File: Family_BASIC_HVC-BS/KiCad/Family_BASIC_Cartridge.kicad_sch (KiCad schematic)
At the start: 19 parts, among them IC1 Working RAM (62256), IC2 Program ROM (27256), IC3 74HCT20, IC4 Character ROM (2764), SW1 BACKUP SW, SW2 RAM BANK SW

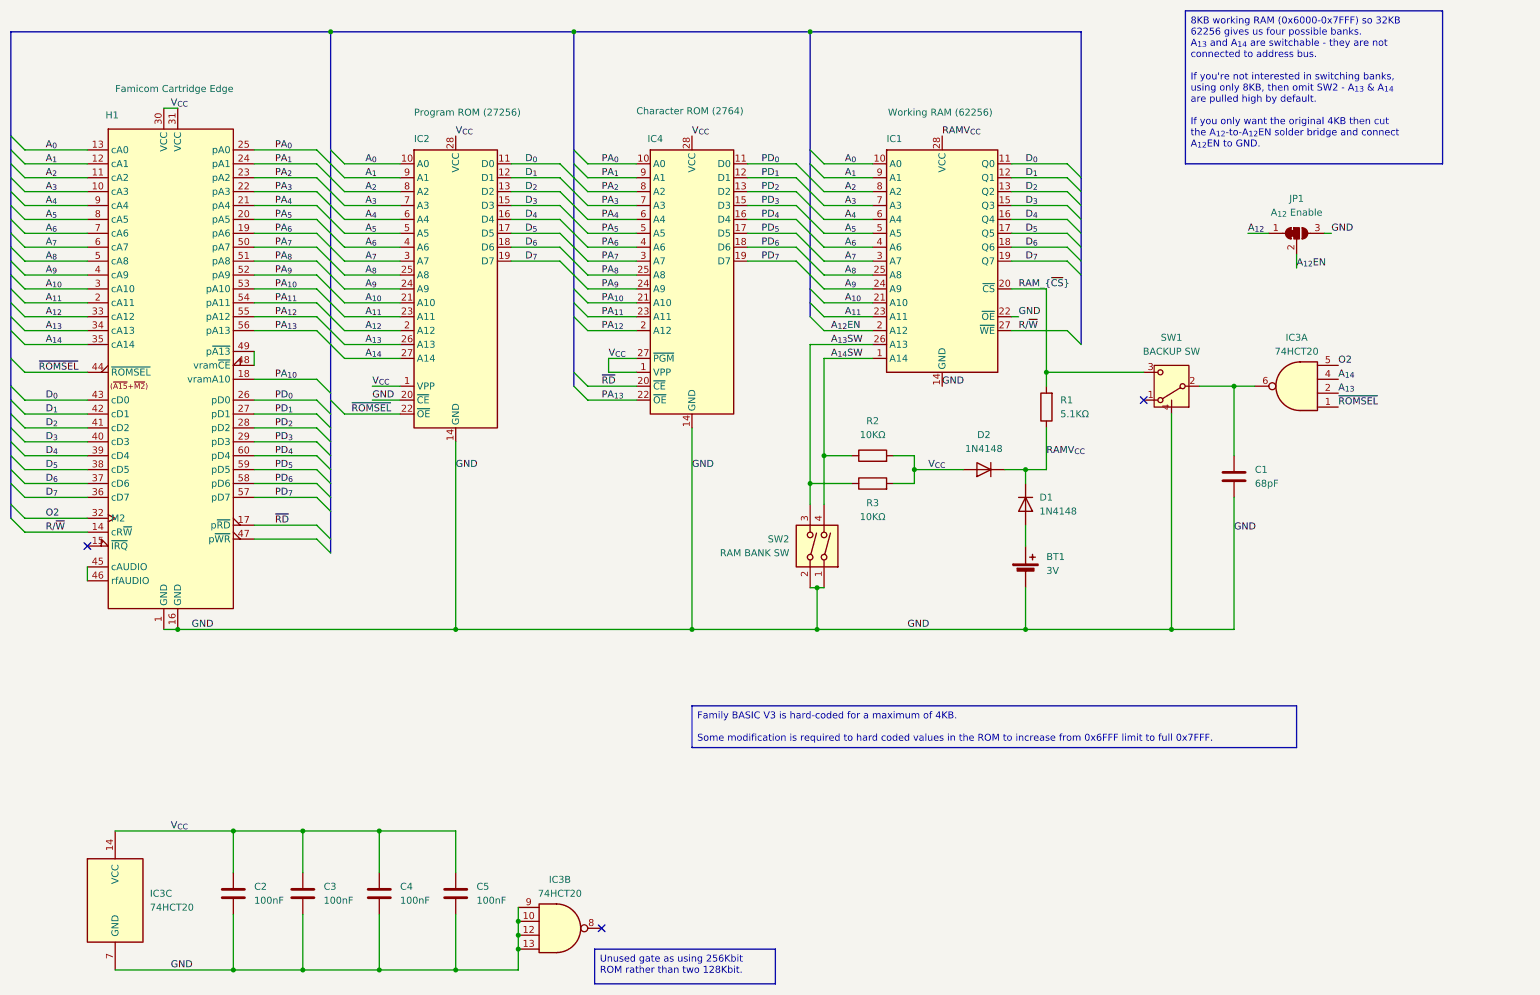
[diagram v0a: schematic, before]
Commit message: Switchable BASIC version with 27512
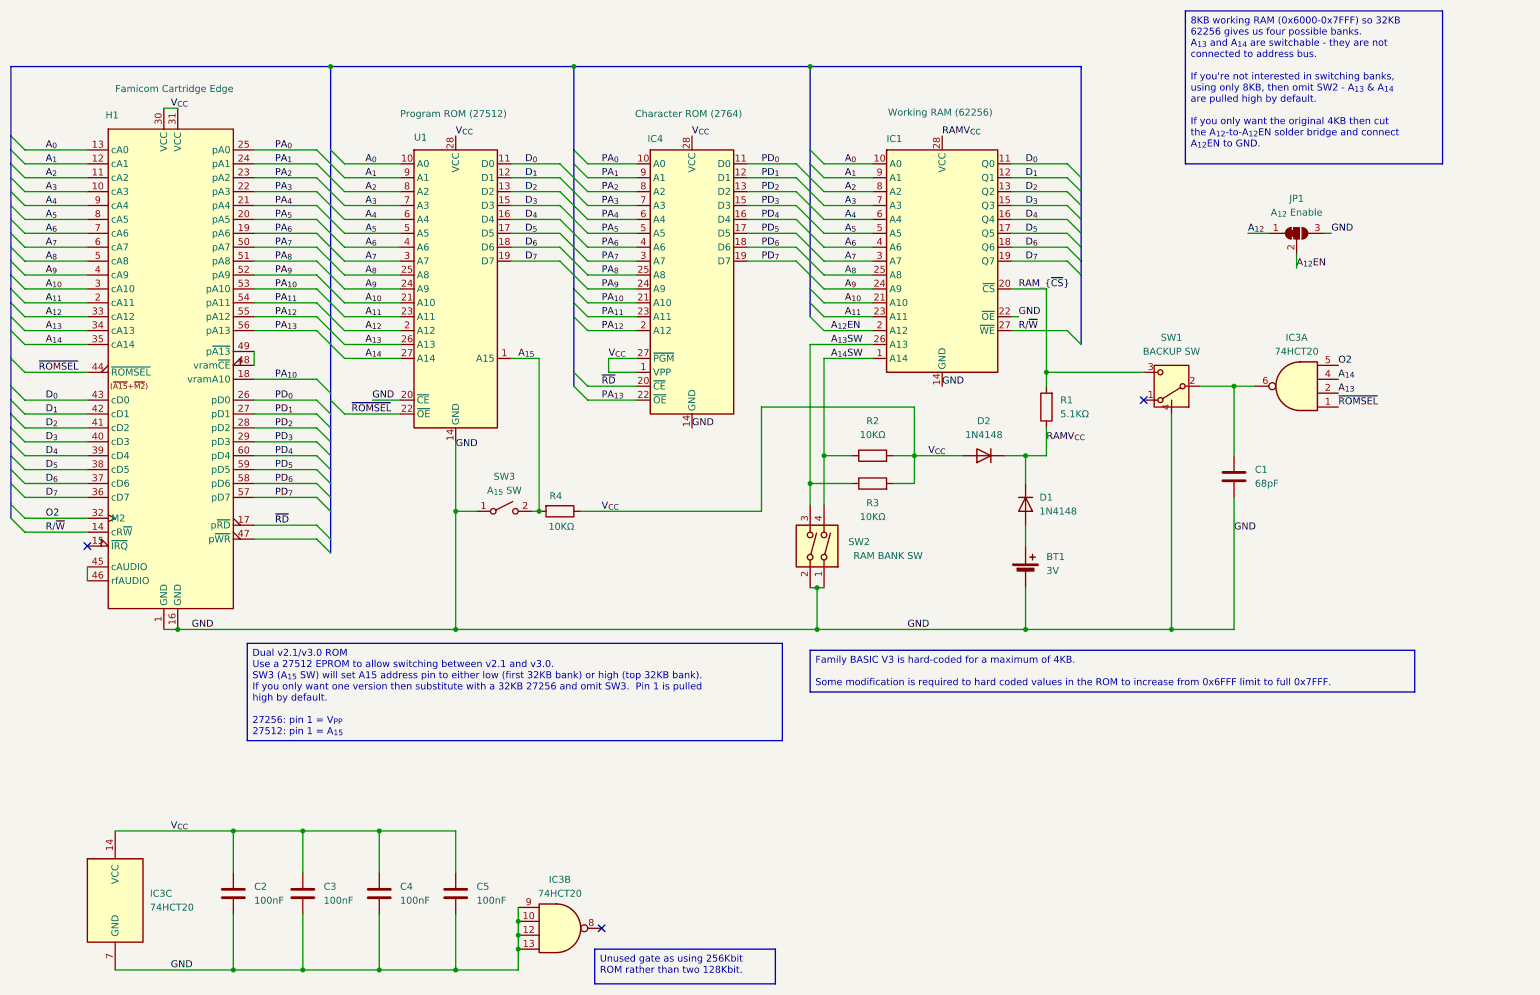
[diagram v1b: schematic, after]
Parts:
- removed IC2: Program ROM (27256), Package_DIP:DIP-28_W15.24mm, symbol Memory_EPROM:27C256
- added R4: 10KΩ, Resistor_THT:R_Axial_DIN0207_L6.3mm_D2.5mm_P7.62mm_Horizontal, symbol Device:R
- added SW3: A_{15} SW, symbol Switch:SW_SPST
- added U1: Program ROM (27512), Package_DIP:DIP-28_W15.24mm, symbol Memory_EPROM:27C512
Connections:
- net A_{0}: now also U1.10 (A0)
- net A_{10}: now also U1.21 (A10)
- net A_{11}: now also U1.23 (A11)
- net A_{12}: now also U1.2 (A12)
- net A_{13}: now also U1.26 (A13)
- net A_{14}: now also U1.27 (A14)
- net A_{1}: now also U1.9 (A1)
- net A_{2}: now also U1.8 (A2)
- net A_{3}: now also U1.7 (A3)
- net A_{4}: now also U1.6 (A4)
- net A_{5}: now also U1.5 (A5)
- net A_{6}: now also U1.4 (A6)
- net A_{7}: now also U1.3 (A7)
- net A_{8}: now also U1.25 (A8)
- net A_{9}: now also U1.24 (A9)
- net D_{0}: now also U1.11 (D0)
- net D_{1}: now also U1.12 (D1)
- net D_{2}: now also U1.13 (D2)
- net D_{3}: now also U1.15 (D3)
- net D_{4}: now also U1.16 (D4)
- net D_{5}: now also U1.17 (D5)
- net D_{6}: now also U1.18 (D6)
- net D_{7}: now also U1.19 (D7)
- net GND: now also SW3.1 (A), U1.14 (GND), U1.20 (~{CE})
- net V_{CC}: now also R4.1, U1.28 (VCC)
- net ~{ROMSEL}: now also U1.22 (~{OE})
- new net A_{15}: R4.2, SW3.2 (B), U1.1 (A15)
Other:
- moved on the sheet: D2

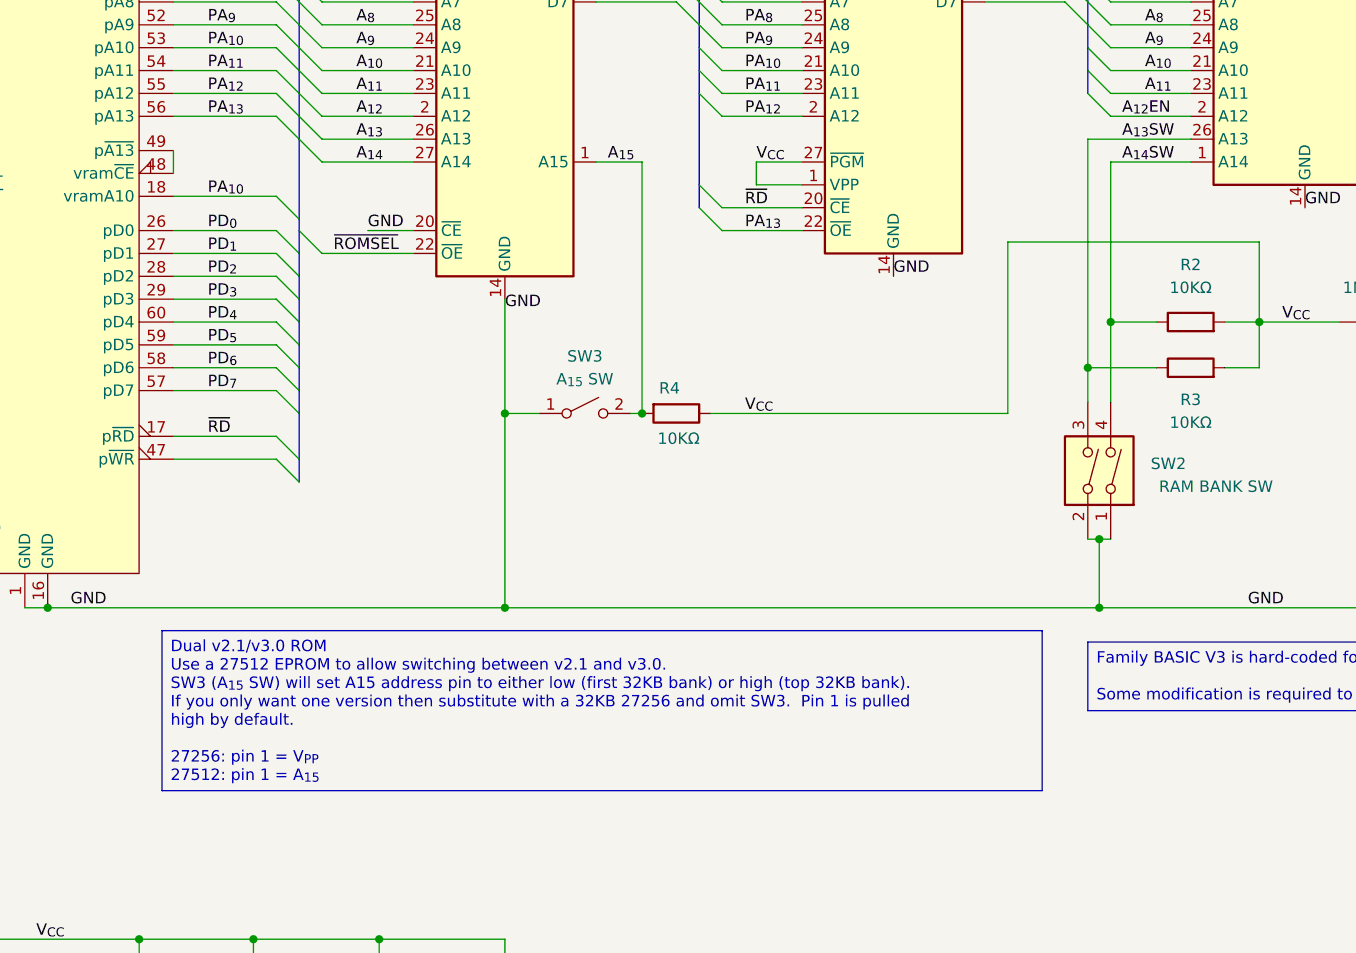
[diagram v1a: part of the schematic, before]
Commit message: Switched PRG ROM to 27512
Switch between v2.1 and v3.0 Family BASIC
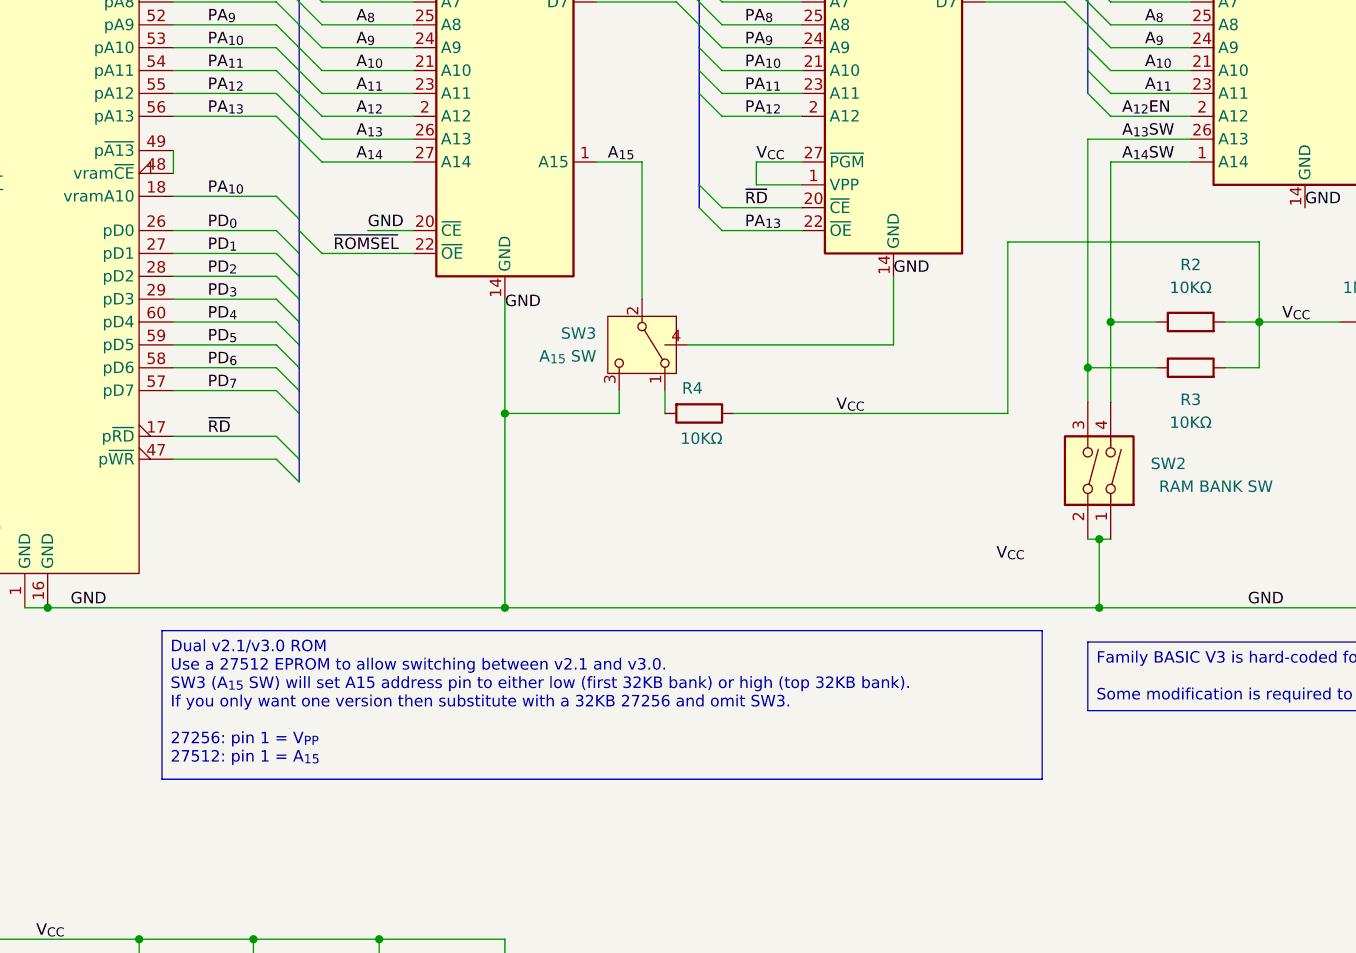
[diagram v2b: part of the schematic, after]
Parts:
- removed SW3: A_{15} SW, symbol Switch:SW_SPST
- added SW3: A_{15} SW, Button_Switch_THT:SW_E-Switch_EG1224_SPDT_Angled, symbol Switch:SW_SPDT
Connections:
- net A_{15}: now also SW3.2 (B); no longer R4.2
- net GND: now also SW3.3 (C), SW3.4 (GND)
- new net: R4.2, SW3.1 (A)
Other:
- moved on the sheet: R4
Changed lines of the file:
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@@
 		(company "Brett Hallen")
 	)
-	(text_box "Dual v2.1/v3.0 ROM\nUse a 27512 EPROM to allow switching between v2.1 and v3.0.\nSW3 (A_{15} SW) will set A15 address pin to either low (first 32KB bank) or high (top 32KB bank).\nIf you only want one version then substitute with a 32KB 27256 and omit SW3.  Pin 1 is pulled high by default.\n\n27256: pin 1 = V_{PP}\n27512: pin 1 = A_{15}"
+	(text_box "Dual v2.1/v3.0 ROM\nUse a 27512 EPROM to allow switching between v2.1 and v3.0.\nSW3 (A_{15} SW) will set A15 address pin to either low (first 32KB bank) or high (top 32KB bank).\nIf you only want one version then substitute with a 32KB 27256 and omit SW3.  \n\n27256: pin 1 = V_{PP}\n27512: pin 1 = A_{15}"
 		(exclude_from_sim no)
 		(at 63.5 133.35 0)
-		(size 97.79 17.78)
+		(size 97.79 16.51)
 		(margins 0.9525 0.9525 0.9525 0.9525)
 		(stroke
@@
 	)
 	(junction
-		(at 116.84 109.22)
-		(diameter 0)
-		(color 0 0 0 0)
-	)
-	(junction
 		(at 50.8 130.81)
 		(diameter 0)
@@
 		)
 	)
-	(wire
-		(pts
-			(xy 116.84 81.28) (xy 116.84 109.22)
-		)
-		(stroke
-			(width 0)
-			(type default)
-		)
-	)
 	(bus
 		(pts
@@
 	(wire
 		(pts
+			(xy 144.78 101.6) (xy 144.78 93.98)
+		)
+		(stroke
+			(width 0)
+			(type default)
+		)
+	)
+	(wire
+		(pts
 			(xy 243.84 106.68) (xy 243.84 130.81)
 		)
@@
 	(wire
 		(pts
-			(xy 115.57 109.22) (xy 116.84 109.22)
-		)
-		(stroke
-			(width 0)
-			(type default)
-		)
-	)
-	(wire
-		(pts
 			(xy 81.28 71.12) (xy 91.44 71.12)
 		)
@@
 	(wire
 		(pts
-			(xy 101.6 109.22) (xy 105.41 109.22)
+			(xy 101.6 109.22) (xy 114.3 109.22)
 		)
 		(stroke
@@
 		)
 	)
+	(wire
+		(pts
+			(xy 127 109.22) (xy 157.48 109.22)
+		)
+		(stroke
+			(width 0)
+			(type default)
+		)
+	)
+	(wire
+		(pts
+			(xy 116.84 81.28) (xy 116.84 96.52)
+		)
+		(stroke
+			(width 0)
+			(type default)
+		)
+	)
 	(bus
 		(pts
@@
 		)
 	)
+	(wire
+		(pts
+			(xy 119.38 109.22) (xy 119.38 106.68)
+		)
+		(stroke
+			(width 0)
+			(type default)
+		)
+	)
 	(bus
 		(pts
@@
 	(wire
 		(pts
-			(xy 124.46 109.22) (xy 157.48 109.22)
+			(xy 111.76 55.88) (xy 120.65 55.88)
 		)
 		(stroke
@@
 	(wire
 		(pts
-			(xy 111.76 55.88) (xy 120.65 55.88)
+			(xy 64.77 106.68) (xy 76.2 106.68)
 		)
 		(stroke
@@
 	(wire
 		(pts
-			(xy 64.77 106.68) (xy 76.2 106.68)
+			(xy 121.92 101.6) (xy 144.78 101.6)
 		)
 		(stroke
@@
 	(wire
 		(pts
+			(xy 114.3 106.68) (xy 114.3 109.22)
+		)
+		(stroke
+			(width 0)
+			(type default)
+		)
+	)
+	(wire
+		(pts
 			(xy 243.84 99.06) (xy 243.84 86.36)
 		)
@@
 	)
 	(label "V_{CC}"
+		(at 138.43 109.22 0)
+		(effects
+			(font
+				(size 1.27 1.27)
+			)
+			(justify left bottom)
+		)
+	)
+	(label "V_{CC}"
 		(at 49.53 35.56 0)
 		(effects
@@
 	)
 	(label "V_{CC}"
-		(at 128.27 109.22 0)
+		(at 156.21 125.73 0)
 		(effects
 			(font
@@
 	(symbol
 		(lib_id "Device:R")
-		(at 120.65 109.22 270)
+		(at 123.19 109.22 270)
 		(unit 1)
 		(exclude_from_sim no)
@@
 		(dnp no)
 		(property "Reference" "R4"
-			(at 119.888 106.426 90)
+			(at 122.428 106.426 90)
 			(effects
 				(font
@@
 		)
 		(property "Value" "10KΩ"
-			(at 120.904 112.014 90)
+			(at 123.444 112.014 90)
 			(effects
 				(font
@@
 		)
 		(property "Footprint" "Resistor_THT:R_Axial_DIN0207_L6.3mm_D2.5mm_P7.62mm_Horizontal"
-			(at 120.65 107.442 90)
+			(at 123.19 107.442 90)
 			(effects
 				(font
@@
 		)
 		(property "Datasheet" "~"
-			(at 120.65 109.22 0)
+			(at 123.19 109.22 0)
 			(effects
 				(font
@@
 		)
 		(property "Description" "Resistor"
-			(at 120.65 109.22 0)
+			(at 123.19 109.22 0)
 			(effects
 				(font
@@
 	)
 	(symbol
-		(lib_id "Switch:SW_SPST")
-		(at 110.49 109.22 0)
+		(lib_id "Switch:SW_SPDT")
+		(at 116.84 101.6 270)
 		(unit 1)
 		(exclude_from_sim no)
@@
 		(fields_autoplaced yes)
 		(property "Reference" "SW3"
-			(at 110.49 102.87 0)
+			(at 111.76 100.3299 90)
 			(effects
 				(font
 					(size 1.27 1.27)
 				)
+				(justify right)
 			)
 		)
 		(property "Value" "A_{15} SW"
-			(at 110.49 105.41 0)
+			(at 111.76 102.8699 90)
 			(effects
 				(font
 					(size 1.27 1.27)
 				)
+				(justify right)
 			)
 		)
-		(property "Footprint" ""
-			(at 110.49 109.22 0)
+		(property "Footprint" "Button_Switch_THT:SW_E-Switch_EG1224_SPDT_Angled"
+			(at 116.84 101.6 0)
 			(effects
 				(font
@@
 		)
 		(property "Datasheet" "~"
-			(at 110.49 109.22 0)
+			(at 109.22 101.6 0)
 			(effects
 				(font
@@
 			)
 		)
-		(property "Description" "Single Pole Single Throw (SPST) switch"
-			(at 110.49 109.22 0)
+		(property "Description" "Switch, single pole double throw"
+			(at 116.84 101.6 0)
 			(effects
 				(font
@@
 			)
 		)
-		(pin "2"
+		(pin "3"
 		)
 		(pin "1"
 		)
+		(pin "2"
+		)
+		(pin "4"
+		)
 		(instances
